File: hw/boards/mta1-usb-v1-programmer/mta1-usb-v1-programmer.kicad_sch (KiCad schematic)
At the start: 24 parts, among them J1 Conn_01x20, J2 Conn_01x20, Q1 AO3400A, Q2 AO3401A, U1 mta1_usb_ch554_pogo, U2 Pico

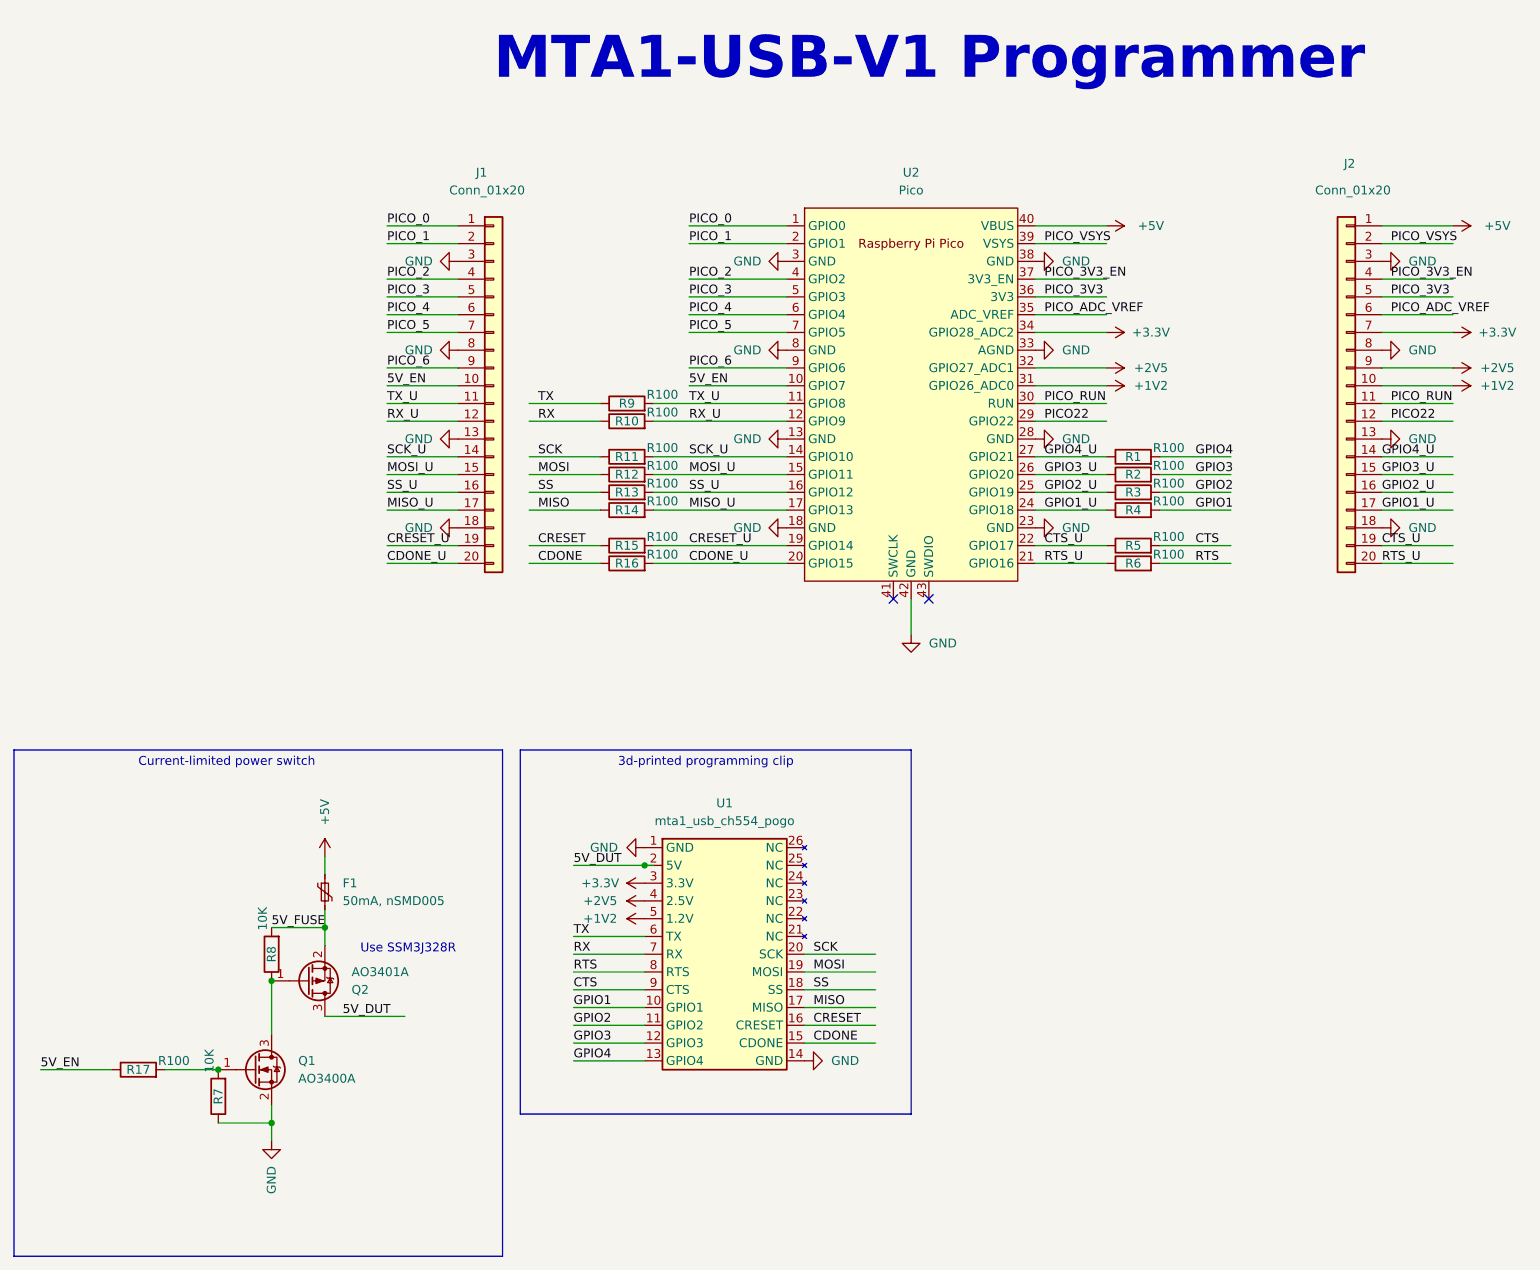
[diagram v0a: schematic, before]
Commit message: mta1-usb-v1-programmer: Add corrected part numbers for OSFC production
* Q1, Q2, F1 part subsititutions
* add mfr/supplier info for all parts
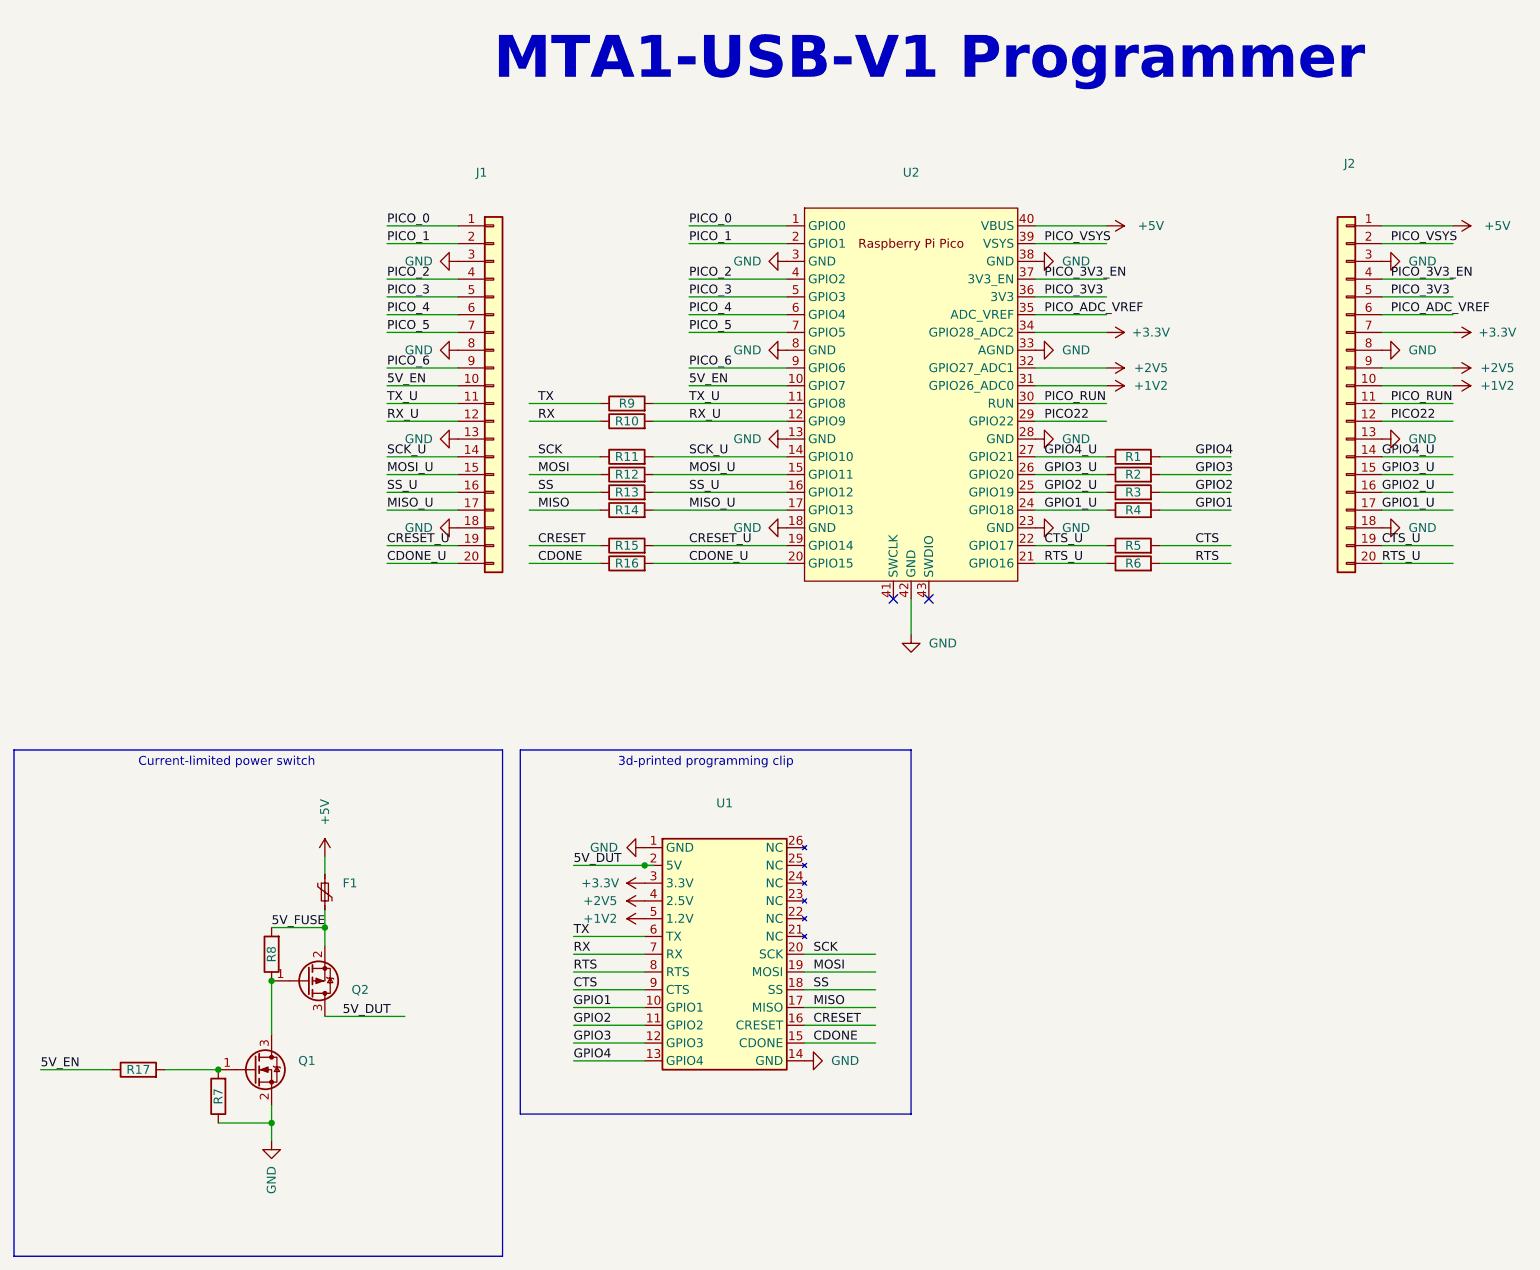
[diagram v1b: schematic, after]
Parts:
- F1: value 50mA, nSMD005 -> (none); footprint Fuse:Fuse_1206_3216Metric -> (none); Manufacturer (none) -> RUILON; Manufacturer Part Number (none) -> SMD1206P005TF; Supplier (none) -> lcsc; Supplier Part Number (none) -> C20797
- J1, J2: value Conn_01x20 -> (none); footprint Connector_PinHeader_2.54mm:PinHeader_1x20_P2.54mm_Vertical -> (none)
- Q1: value AO3400A -> (none); footprint Package_TO_SOT_SMD:SOT-23 -> (none); Manufacturer (none) -> winsok; Manufacturer Part Number (none) -> WST3400A; Supplier (none) -> lcsc; Supplier Part Number (none) -> C2758406
- Q2: value AO3401A -> (none); footprint Package_TO_SOT_SMD:SOT-23 -> (none); Extended Value (none) -> 1%,1/16W; Manufacturer (none) -> jjm; Manufacturer Part Number (none) -> JMTL3401A; Supplier (none) -> lcsc; Supplier Part Number (none) -> C394037
- R1, R10, R11, R12, R13, R14, R15, R16, R17, R2, R3, R4, R5, R6, R9: value R100 -> (none); footprint mta1:ERJ2G(0402)_L -> (none); Manufacturer (none) -> yageo; Manufacturer Part Number (none) -> AF0402FR-07100RL; Supplier (none) -> Digikey; Supplier Part Number (none) -> 13-AF0402FR-07100RLTR-ND
- R7, R8: value 10K -> (none); footprint mta1:ERJ2G(0402)_L -> (none); Extended Value (none) -> 1%,1/16W; Manufacturer (none) -> yageo; Manufacturer Part Number (none) -> AT0402FRE0710KL; Supplier (none) -> Digikey; Supplier Part Number (none) -> YAG2104TR-ND
- U1: value mta1_usb_ch554_pogo -> (none); footprint mta1-usb:mta1_usb_ch554_pogo -> (none); Manufacturer (none) -> blinkinlabs
- U2: value Pico -> (none); footprint RPi_Pico:RPi_Pico_SMD_TH -> (none); Manufacturer (none) -> Raspberry Pi; Manufacturer Part Number (none) -> SC0915; Supplier (none) -> Digikey; Supplier Part Number (none) -> 2648-SC0915TR-ND
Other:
- note removed: "Use SSM3J328R"
